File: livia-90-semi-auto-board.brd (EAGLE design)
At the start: 60.8 x 75.6 mm, 37 parts, among them K1 RT444012, K2 RT444012, K3 G5LE, Q1 200mA/40V, Q2 200mA/40V, Q3 200mA/40V, U1 12VDC

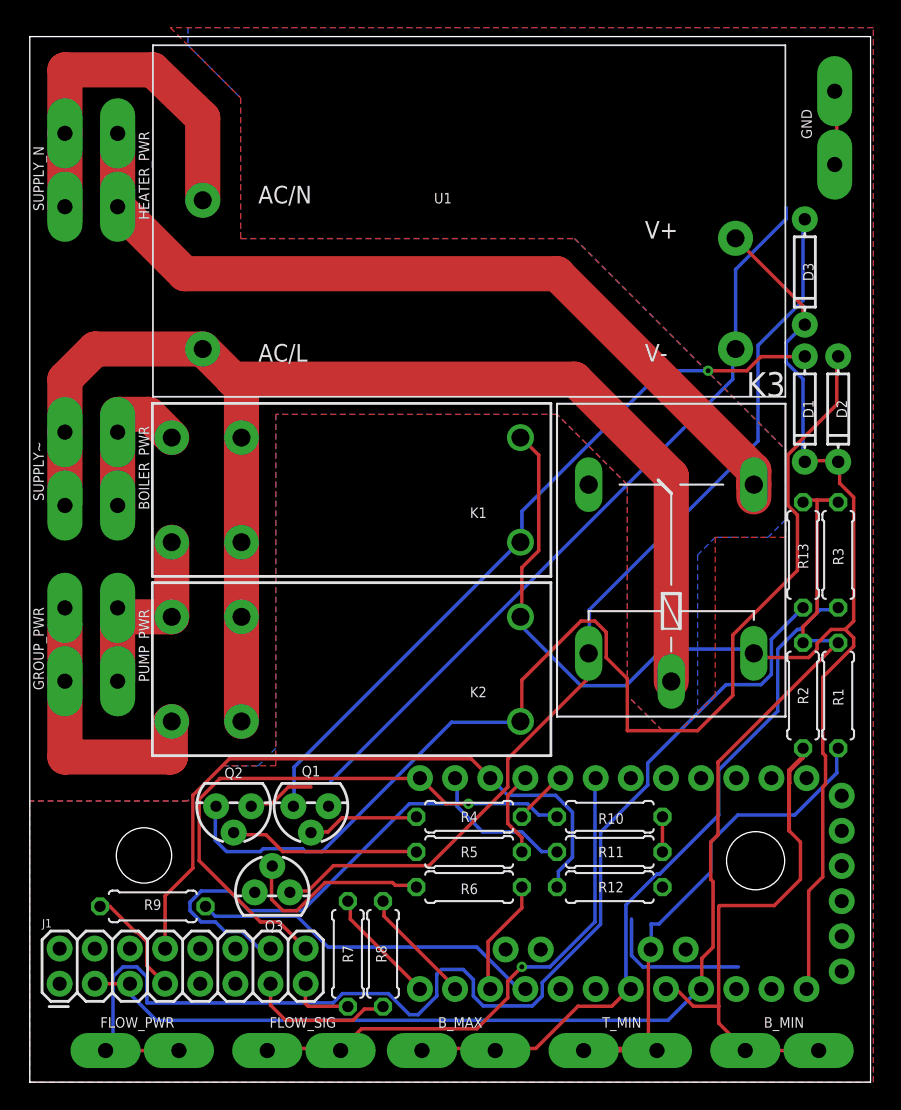
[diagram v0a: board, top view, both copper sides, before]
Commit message: added temperature 1line output. This board was sent to production
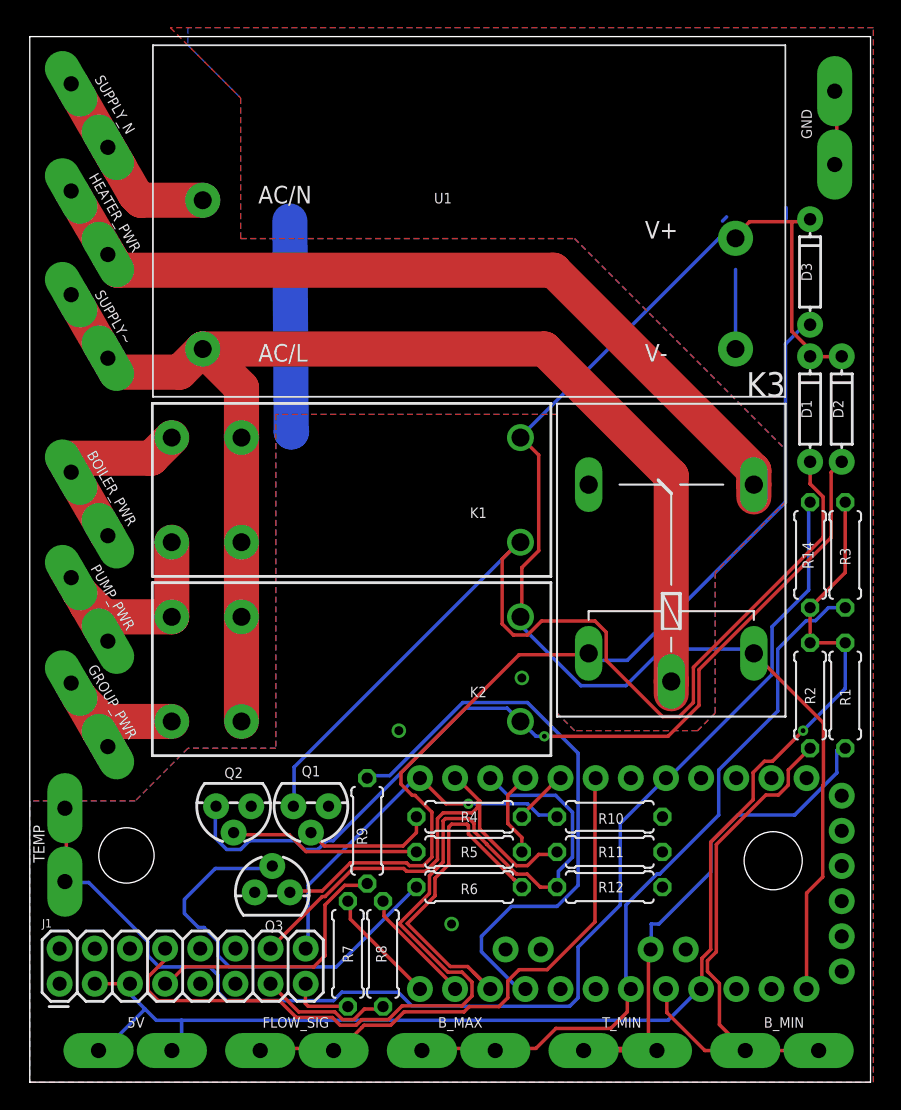
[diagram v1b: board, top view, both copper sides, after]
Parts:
- removed FLOW_PWR: (no value), con-faston:F061.040
- removed R13: (no value), rcl:0207/7
- added 5V, TEMP: (no value), con-faston:F061.040
- added R14: 4.7k, rcl:0207/7
- moved R9 16.4 mm to (24.4, 18.2), turned to 90 degrees
- moved SUPPLY~ 10.4 mm to (4.32, 54.6), turned to 120 degrees
- moved GROUP_PWR 5.38 mm to (4.32, 26.5), turned to 300 degrees
- moved SUPPLY_N 4.32 mm to (4.32, 69.8), turned to 120 degrees
- moved HEATER_PWR 4.32 mm to (4.32, 62.1), turned to 120 degrees
- moved BOILER_PWR 3.25 mm to (4.32, 41.8), turned to 120 degrees
- moved PUMP_PWR 3.25 mm to (4.32, 34.2), turned to 120 degrees
- moved FLOW_SIG 0.51 mm to (19.3, 2.29)
- moved R1 0.51 mm to (58.9, 27.9)
- moved R2 0.51 mm to (56.4, 27.9)
- moved R3 0.51 mm to (58.9, 38.1)
- moved D1 0.38 mm to (56.4, 48.6), turned to 90 degrees
- moved D3 0.38 mm to (56.4, 58.5), turned to 90 degrees
- moved D2 0.25 mm to (58.7, 48.6), turned to 90 degrees
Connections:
- removed net N$3: FLOW_PWR.A1, FLOW_PWR.A2, R13.1
- new net TEMP: B1.5, R14.2, TEMP.A1, TEMP.A2
- net VCC: now also 5V.A1, 5V.A2, R14.1; no longer R13.2
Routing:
- net TEMP: track 0.00 -> 91.2 mm
- net N$3: track 87.0 -> 0.00 mm
- net GND: track 80.5 -> 29.3 mm, vias 0 -> 3
- net SUPPLY_N: track 38.4 -> 16.0 mm
- net STOP_BTN: track 47.9 -> 69.1 mm
- net N$20: track 53.3 -> 73.1 mm, vias 1 -> 0
- net N$18: track 84.8 -> 66.0 mm, vias 0 -> 1
- net STOP_LED: track 25.6 -> 42.7 mm
- net HEAT: track 8.43 -> 25.5 mm
- net N$13: track 14.2 -> 29.8 mm
- net SNGL_BTN: track 42.4 -> 27.2 mm
- net N$14: track 8.02 -> 19.8 mm
- net DBL_BTN: track 41.7 -> 33.2 mm
- net N$10: track 14.6 -> 21.3 mm
- net N$2: track 21.3 -> 15.1 mm
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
